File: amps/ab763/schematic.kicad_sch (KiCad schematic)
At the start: 120 parts, among them T1 125P33A, T2 125C3A, T3 125A1A, T4 125A20B

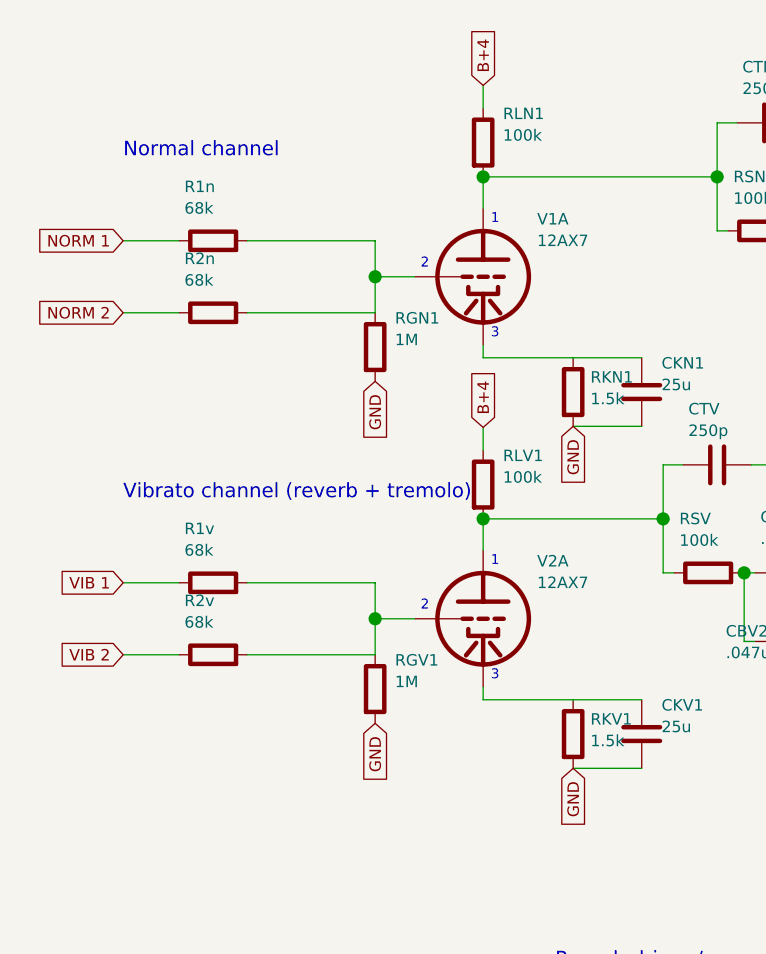
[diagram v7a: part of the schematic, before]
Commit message: AB763 Deluxe: input leaks at jack 1's tip (V1 audit carry-over)
C-FD hangs each channel's 1M from jack 1's tip, jack side of its lower
68k (schematic 6070x4274, Normal crop 200,780,800,1500; the Vibrato pair
is drawn the same at 200,1900,800,2600): jack 2's contact -> jack 1's
tip, jack 1's contact -> ground. The grid junction between the two 68ks
carries nothing else. The sheet had both leaks on the grid bus.
R1n/R1v are declared series_bridge so the netlist's RGN1 GN1 0 and
RGV1 GV1 0 still bind (the AA1164 / AB763 Twin idiom, 1bab462). The
board already mounts both leaks at the jacks (net_map.netlist_unplaced).
BOM roles, the jack note and the circuit story are corrected; the two
channel headings move up 3 mm to clear the new ground flags. No DC node
moves.

Co-Authored-By: Claude Opus 5.5 <noreply@anthropic.com>
Claude-Session: https://claude.ai/code/session_01KBMfdh37HmCL2iWcBiL5J1
Signed-off-by: AnalogMaker <theanalogmaker@gmail.com>
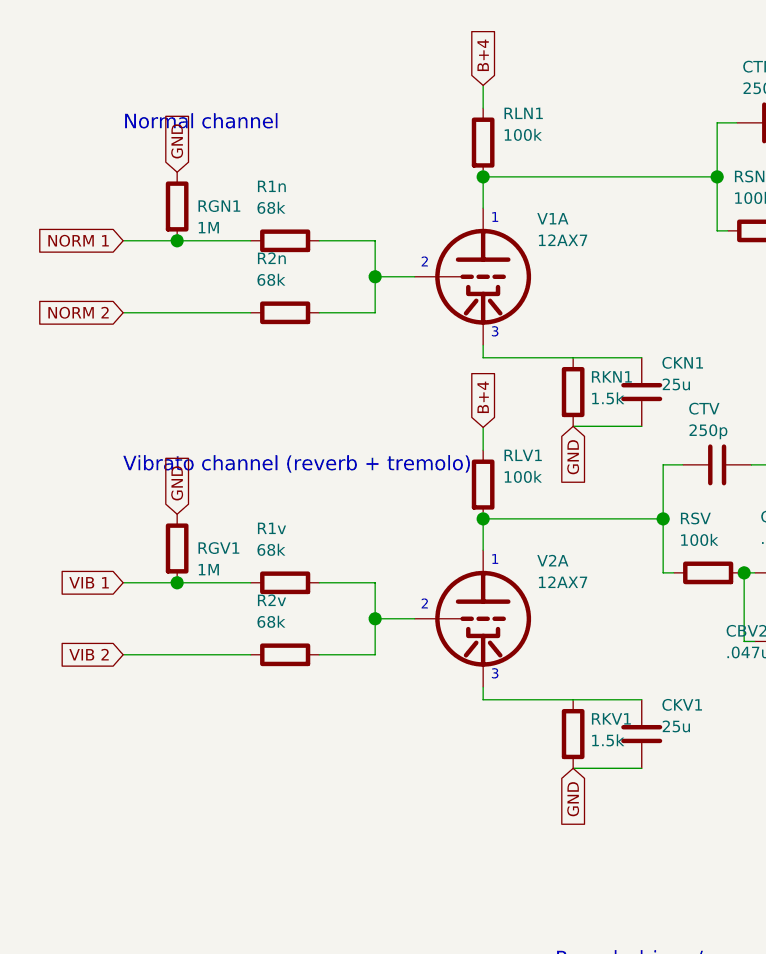
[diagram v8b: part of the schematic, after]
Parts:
- removed C10: 16u, symbol cx:C
- removed C2, CBV: .1u, symbol cx:C
- removed CB1, CKRD, CKTO2: 25u, symbol cx:C
- removed CBV2: .047u, symbol cx:C
- removed CRS: 500p, symbol cx:C
- removed CTV: 250p, symbol cx:C
- removed R2v: 68k, symbol cx:R
- removed RGD2, RGL1, RGL2: 220k, symbol cx:R
- removed RLAMP, RLR1, RLV2: 100k, symbol cx:R
- removed RLPA: 82k 5%, symbol cx:R
- removed RNF2: 47, symbol cx:R
- removed RTOG2: 1M, symbol cx:R
- removed VRSPD: 3M speed, symbol cx:POT
- added C1: .1u, symbol cx:C
- added CBRV: 47p, symbol cx:C
- added CTO1: .01u, symbol cx:C
- added OPTO: roach, symbol cx:OPTO
- added R7s, R8s: 1.5k, symbol cx:R
- added RBAL: 10k, symbol cx:R
- added RGD1: 3.3M, symbol cx:R
- added RGV1: 1M, symbol cx:R
- added RKR1, RKV2: 820, symbol cx:R
- added RLPB: 100k 5%, symbol cx:R
- added T2: 125C3A, symbol cx:CHOKE
- added T3: 125A1A, symbol cx:OT_PP
- added T4: 125A20B, symbol cx:OT_SE
- added V4A, V6B: 12AT7, symbol cx:TRIODE
- added VRBV: 250k bass, symbol cx:POT
- added VRINT: 50k int, symbol cx:POT
- added VRTV: 250k treb, symbol cx:POT
- C10: renamed from T2; value 125C3A -> 16u; symbol cx:CHOKE -> cx:C
- C2: renamed from R7s; value 1.5k -> .1u; symbol cx:R -> cx:C
- CB1: renamed from VRBAL; value 10k bal -> 25u; symbol cx:POT -> cx:C
- CBV: renamed from VRBV; value 250k bass -> .1u; symbol cx:POT -> cx:C
- CBV2: renamed from RSLV; value 6.8k -> .047u; symbol cx:R -> cx:C
- CKRD: renamed from T4; value 125A20B -> 25u; symbol cx:OT_SE -> cx:C
- CKTO2: renamed from OPTO; value roach -> 25u; symbol cx:OPTO -> cx:C
- CPIA: renamed from V6B; value 12AT7 -> .001u; symbol cx:TRIODE -> cx:C; Basing_unit 1 -> (none)
- CRS: renamed from V4A; value 12AT7 -> 500p; symbol cx:TRIODE -> cx:C
- CTV: renamed from VRTV; value 250k treb -> 250p; symbol cx:POT -> cx:C
- R2v: renamed from RGV1; value 1M -> 68k
- RGD2: renamed from RGD1; value 3.3M -> 220k
- RGL1: renamed from RS1; value 470 1W -> 220k
- RGL2: renamed from RS2; value 470 1W -> 220k
- RLAMP: renamed from VRINT; value 50k int -> 100k; symbol cx:POT -> cx:R
- RLPA: renamed from RLPB; value 100k 5% -> 82k 5%
- RLR1: renamed from RKR1; value 820 -> 100k
- RLV2: renamed from RKV2; value 820 -> 100k
- RNF2: renamed from C1; value .1u -> 47; symbol cx:C -> cx:R
- RS1: renamed from R8s; value 1.5k -> 470 1W
- RS2: renamed from T3; value 125A1A -> 470 1W; symbol cx:OT_PP -> cx:R
- RSLV: renamed from VRVV; value 1M vol -> 6.8k; symbol cx:POT -> cx:R
- RTO1: renamed from CPIA; value .001u -> 100k; symbol cx:C -> cx:R
- RTOG3: renamed from CTO1; value .01u -> 1M; symbol cx:C -> cx:R
- VRBAL: renamed from RBAL; value 10k -> 10k bal; symbol cx:R -> cx:POT
- VRSPD: renamed from RTO1; value 100k -> 3M speed; symbol cx:R -> cx:POT
- VRVV: renamed from CBRV; value 47p -> 1M vol; symbol cx:C -> cx:POT
- renumbered RTOG3 to RTOG2
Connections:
- net -35V: now also RGL1.2, RGL2.2, VRBAL.2 (W); no longer CB1.2 (W)
- net B+1: now also T2.1, T3.2 (CT); no longer RS2.2 (CT)
- net B+2: now also RLAMP.1, RS1.2, RS2.2, T2.2; no longer C10.2, RGL1.2, RGL2.2
- net B+3: now also RLPB.1
- net B+4: now also RLR1.1, RLV2.1
- net BIAS RAW: now also VRBAL.1
- net GND: now also C10.2, CB1.2, CKRD.2, CKTO2.2, RGD2.2, RGN1.1, RNF2.2, RSLV.2, RTO1.2, VRVV.3, OPTO.4 (P2), RBAL.2, RGV1.1, RKR1.2, RKV2.2, T3.5 (SEC_C), T4.4 (SEC_C), VRINT.1; no longer CBV2.2, CKRD.4 (SEC_C), CKTO2.4 (P2), R2v.2, RGN1.2, RLAMP.1, RLR1.2, RLV2.2, RS2.5 (SEC_C), RSLV.3, VRBAL.2, VRSPD.2
- net KA: now also RKV2.1; no longer RLV2.1
- net KE: now also RKR1.1; no longer RLR1.1
- net LFO: now also RTOG2.2, CTO1.1; no longer RTOG3.1
- net MIXG: now also RGD2.1, RGD1.2; no longer RGD2.2
- net NORM 1: now also RGN1.2
- net PIG: now also CPIA.1; no longer RTO1.1
- net REVERB TANK: now also T4.3 (SEC_H); no longer CKRD.3 (SEC_H)
- net RVSEND: now also CRS.1, RGD1.1; no longer RGD2.1
- net SPEED: now also VRSPD.1
- net SPKR: now also T3.4 (SEC_H); no longer RS2.4 (SEC_H)
- net TREM: now also VRINT.3; no longer RLAMP.3
- net VIB 1: now also RGV1.2
- net VIB 2: now also R2v.1
- net VIB PEDAL: now also RTOG3.1
- net at RKTO2.1, V5B.3 (K): now also CKTO2.1
- net at RGPA.1, V6A.2 (G): now also CPIA.2; no longer RTO1.2
- net at CPIB.1, RNFB.2, RT2.2: now also RNF2.1
- net at CCV2.1, V2B.1 (P): now also RLV2.2
- net at CCR1.1, V3B.1 (P): now also RLR1.2
- net at RS2.1: now also V8.3 (G2); no longer V7.1 (P)
- net at V8.1 (P): now also T3.3 (PRI_B); no longer RS2.3 (PRI_B)
- net at RLPA.2: now also V6A.1 (P), C1.1; no longer CPIA.1 (P)
- net at RS1.1: now also V7.3 (G2)
- net at RGL2.1: now also C2.2, R8s.1; no longer V8.3 (G2)
- net at RLV1.2, RSV.1, V2A.1 (P): now also CTV.1
- net at R1n.2, R2n.2, V1A.2 (G): no longer RGN1.1
- net at CBV2.1: now also CBV.1, RSV.2; no longer CBV.3
- net at CPIB.2, RGPB.2: now also V6B.2 (G); no longer CPIA.2 (G)
- net at R1v.2, V2A.2 (G): now also R2v.2; no longer R2v.1
- net at RTO10.2, V5B.1 (P): now also OPTO.2 (L2); no longer CKTO2.2 (L2)
- net at V8.2 (G1): now also R8s.2; no longer RS1.2
- net at V4B.1 (P): now also V4A.1 (P); no longer CRS.1 (P)
- net at CRS.2, RGRD.1, V4B.2 (G): now also V4A.2 (G)
- net at RKRD.1, V4B.3 (K): now also CKRD.1, V4A.3 (K); no longer CRS.3 (K)
- net at C2.1: now also RLPB.2, V6B.1 (P); no longer RNF2.2
- net at V7.2 (G1): now also R7s.2; no longer C2.2
- net at V2B.2 (G), VRVV.2 (W): now also CBRV.2; no longer RSLV.2 (W)
- net at RGL1.1: now also C1.2, R7s.1; no longer V7.3 (G2)
- net at CBV.2: now also VRBV.1, VRTV.3
- net at RTOG3.2, V5A.2 (G): now also CTO1.2; no longer RTOG2.2
- net at RSLV.1: now also CBV2.2, VRBV.3; no longer VRVV.1
- net at RLAMP.2: now also OPTO.1 (L1); no longer CKTO2.3 (P1)
- net at RTAIL.2, V6A.3 (K): now also V6B.3 (K); no longer CPIA.3 (K)
- net at CTV.2: now also VRTV.1
- new net: OPTO.3 (P1), VRINT.2 (W)
- new net: CBRV.1, VRVV.1
- new net: RTO1.1, VRSPD.2 (W), VRSPD.3
- new net: T3.1 (PRI_A), V7.1 (P)
- new net: RBAL.1, VRBAL.3
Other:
- moved on the sheet: R1n, R2v, RGD2, RGL1, RGL2, RLPA, RLR1, RLV2, RS1, RTOG2
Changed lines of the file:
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@@
     (comment 2 "CC-BY-SA 4.0 · circuitcodex.com")
     (comment 3 "Values read from: https://el34world.com/charts/Schematics/files/Fender/Fender_deluxe_reverb_ab763.pdf"))
-  (text "Normal channel" (at 19.6088 24.278 0)
+  (text "Normal channel" (at 19.6088 21.278 0)
     (effects (font (size 1.6 1.6)) (justify left)))
   (global_label "NORM 1" (shape input) (at 19.6088 34.278 180)
@@
   (global_label "NORM 2" (shape input) (at 19.6088 42.278 180)
     (effects (font (size 1.27 1.27)) (justify right)))
-  (symbol (lib_id "cx:R") (at 29.6088 34.278 90) (unit 1)
-    (in_bom yes) (on_board yes)
-    (property "Reference" "R1n" (at 26.4088 28.278 270) (effects (font (size 1.27 1.27)) (justify left)))
-    (property "Value" "68k" (at 26.4088 30.678 270) (effects (font (size 1.27 1.27)) (justify left))))
-  (wire (pts (xy 19.6088 34.278) (xy 25.7988 34.278))
-    (stroke (width 0) (type default)))
-  (wire (pts (xy 33.4188 34.278) (xy 47.6088 34.278))
-    (stroke (width 0) (type default)))
-  (symbol (lib_id "cx:R") (at 29.6088 42.278 90) (unit 1)
-    (in_bom yes) (on_board yes)
-    (property "Reference" "R2n" (at 26.4088 36.278 270) (effects (font (size 1.27 1.27)) (justify left)))
-    (property "Value" "68k" (at 26.4088 38.678 270) (effects (font (size 1.27 1.27)) (justify left))))
-  (wire (pts (xy 19.6088 42.278) (xy 25.7988 42.278))
-    (stroke (width 0) (type default)))
-  (wire (pts (xy 33.4188 42.278) (xy 47.6088 42.278))
+  (symbol (lib_id "cx:R") (at 37.6088 34.278 90) (unit 1)
+    (in_bom yes) (on_board yes)
+    (property "Reference" "R1n" (at 34.4088 28.278 270) (effects (font (size 1.27 1.27)) (justify left)))
+    (property "Value" "68k" (at 34.4088 30.678 270) (effects (font (size 1.27 1.27)) (justify left))))
+  (wire (pts (xy 19.6088 34.278) (xy 25.6088 34.278))
+    (stroke (width 0) (type default)))
+  (wire (pts (xy 25.6088 34.278) (xy 33.7988 34.278))
+    (stroke (width 0) (type default)))
+  (wire (pts (xy 41.4188 34.278) (xy 47.6088 34.278))
+    (stroke (width 0) (type default)))
+  (junction (at 25.6088 34.278) (diameter 1.46) (color 0 0 0 0))
+  (symbol (lib_id "cx:R") (at 25.6088 30.468 0) (unit 1)
+    (in_bom yes) (on_board yes)
+    (property "Reference" "RGN1" (at 27.8088 30.468 0) (effects (font (size 1.27 1.27)) (justify left)))
+    (property "Value" "1M" (at 27.8088 32.868 0) (effects (font (size 1.27 1.27)) (justify left))))
+  (global_label "GND" (shape input) (at 25.6088 26.658 90)
+    (effects (font (size 1.27 1.27)) (justify left)))
+  (symbol (lib_id "cx:R") (at 37.6088 42.278 90) (unit 1)
+    (in_bom yes) (on_board yes)
+    (property "Reference" "R2n" (at 34.4088 36.278 270) (effects (font (size 1.27 1.27)) (justify left)))
+    (property "Value" "68k" (at 34.4088 38.678 270) (effects (font (size 1.27 1.27)) (justify left))))
+  (wire (pts (xy 19.6088 42.278) (xy 33.7988 42.278))
+    (stroke (width 0) (type default)))
+  (wire (pts (xy 41.4188 42.278) (xy 47.6088 42.278))
     (stroke (width 0) (type default)))
   (wire (pts (xy 47.6088 34.278) (xy 47.6088 38.278))
@@
     (stroke (width 0) (type default)))
   (junction (at 47.6088 38.278) (diameter 1.46) (color 0 0 0 0))
-  (symbol (lib_id "cx:R") (at 47.6088 46.088 0) (unit 1)
-    (in_bom yes) (on_board yes)
-    (property "Reference" "RGN1" (at 49.8088 42.888 0) (effects (font (size 1.27 1.27)) (justify left)))
-    (property "Value" "1M" (at 49.8088 45.288 0) (effects (font (size 1.27 1.27)) (justify left))))
-  (global_label "GND" (shape input) (at 47.6088 49.898 270)
-    (effects (font (size 1.27 1.27)) (justify right)))
   (symbol (lib_id "cx:TRIODE") (at 59.6088 38.278 0) (unit 1)
     (in_bom yes) (on_board yes)
@@
   (global_label "PIG" (shape input) (at 237.609 27.178 0)
     (effects (font (size 1.27 1.27)) (justify left)))
-  (text "Vibrato channel (reverb + tremolo)" (at 19.6088 62.278 0)
+  (text "Vibrato channel (reverb + tremolo)" (at 19.6088 59.278 0)
     (effects (font (size 1.6 1.6)) (justify left)))
   (global_label "VIB 1" (shape input) (at 19.6088 72.278 180)
@@
   (global_label "VIB 2" (shape input) (at 19.6088 80.278 180)
     (effects (font (size 1.27 1.27)) (justify right)))
-  (symbol (lib_id "cx:R") (at 29.6088 72.278 90) (unit 1)
-    (in_bom yes) (on_board yes)
-    (property "Reference" "R1v" (at 26.4088 66.278 270) (effects (font (size 1.27 1.27)) (justify left)))
-    (property "Value" "68k" (at 26.4088 68.678 270) (effects (font (size 1.27 1.27)) (justify left))))
-  (wire (pts (xy 19.6088 72.278) (xy 25.7988 72.278))
-    (stroke (width 0) (type default)))
-  (wire (pts (xy 33.4188 72.278) (xy 47.6088 72.278))
-    (stroke (width 0) (type default)))
-  (symbol (lib_id "cx:R") (at 29.6088 80.278 90) (unit 1)
-    (in_bom yes) (on_board yes)
-    (property "Reference" "R2v" (at 26.4088 74.278 270) (effects (font (size 1.27 1.27)) (justify left)))
-    (property "Value" "68k" (at 26.4088 76.678 270) (effects (font (size 1.27 1.27)) (justify left))))
-  (wire (pts (xy 19.6088 80.278) (xy 25.7988 80.278))
-    (stroke (width 0) (type default)))
-  (wire (pts (xy 33.4188 80.278) (xy 47.6088 80.278))
+  (symbol (lib_id "cx:R") (at 37.6088 72.278 90) (unit 1)
+    (in_bom yes) (on_board yes)
+    (property "Reference" "R1v" (at 34.4088 66.278 270) (effects (font (size 1.27 1.27)) (justify left)))
+    (property "Value" "68k" (at 34.4088 68.678 270) (effects (font (size 1.27 1.27)) (justify left))))
+  (wire (pts (xy 19.6088 72.278) (xy 25.6088 72.278))
+    (stroke (width 0) (type default)))
+  (wire (pts (xy 25.6088 72.278) (xy 33.7988 72.278))
+    (stroke (width 0) (type default)))
+  (wire (pts (xy 41.4188 72.278) (xy 47.6088 72.278))
+    (stroke (width 0) (type default)))
+  (junction (at 25.6088 72.278) (diameter 1.46) (color 0 0 0 0))
+  (symbol (lib_id "cx:R") (at 25.6088 68.468 0) (unit 1)
+    (in_bom yes) (on_board yes)
+    (property "Reference" "RGV1" (at 27.8088 68.468 0) (effects (font (size 1.27 1.27)) (justify left)))
+    (property "Value" "1M" (at 27.8088 70.868 0) (effects (font (size 1.27 1.27)) (justify left))))
+  (global_label "GND" (shape input) (at 25.6088 64.658 90)
+    (effects (font (size 1.27 1.27)) (justify left)))
+  (symbol (lib_id "cx:R") (at 37.6088 80.278 90) (unit 1)
+    (in_bom yes) (on_board yes)
+    (property "Reference" "R2v" (at 34.4088 74.278 270) (effects (font (size 1.27 1.27)) (justify left)))
+    (property "Value" "68k" (at 34.4088 76.678 270) (effects (font (size 1.27 1.27)) (justify left))))
+  (wire (pts (xy 19.6088 80.278) (xy 33.7988 80.278))
+    (stroke (width 0) (type default)))
+  (wire (pts (xy 41.4188 80.278) (xy 47.6088 80.278))
     (stroke (width 0) (type default)))
   (wire (pts (xy 47.6088 72.278) (xy 47.6088 76.278))
@@
     (stroke (width 0) (type default)))
   (junction (at 47.6088 76.278) (diameter 1.46) (color 0 0 0 0))
-  (symbol (lib_id "cx:R") (at 47.6088 84.088 0) (unit 1)
-    (in_bom yes) (on_board yes)
-    (property "Reference" "RGV1" (at 49.8088 80.888 0) (effects (font (size 1.27 1.27)) (justify left)))
-    (property "Value" "1M" (at 49.8088 83.288 0) (effects (font (size 1.27 1.27)) (justify left))))
-  (global_label "GND" (shape input) (at 47.6088 87.898 270)
-    (effects (font (size 1.27 1.27)) (justify right)))
   (symbol (lib_id "cx:TRIODE") (at 59.6088 76.278 0) (unit 1)
     (in_bom yes) (on_board yes)
